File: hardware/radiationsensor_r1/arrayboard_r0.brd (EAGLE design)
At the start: 131.7 x 72.1 mm, 25 parts, among them CN0 RADIATION-SENSOR-REV1, CN1 RADIATION-SENSOR-REV1, CN10 RADIATION-SENSOR-REV1, CN11 RADIATION-SENSOR-REV1, CN12 RADIATION-SENSOR-REV1, CN13 RADIATION-SENSOR-REV1, CN14 RADIATION-SENSOR-REV1, CN15 RADIATION-SENSOR-REV1, CN16 2524-, CN17 22-23-2041, CN2 RADIATION-SENSOR-REV1, CN3 RADIATION-SENSOR-REV1, CN4 RADIATION-SENSOR-REV1, CN5 RADIATION-SENSOR-REV1, CN6 RADIATION-SENSOR-REV1, CN7 RADIATION-SENSOR-REV1, CN8 RADIATION-SENSOR-REV1, CN9 RADIATION-SENSOR-REV1, U1 MCP23017SS

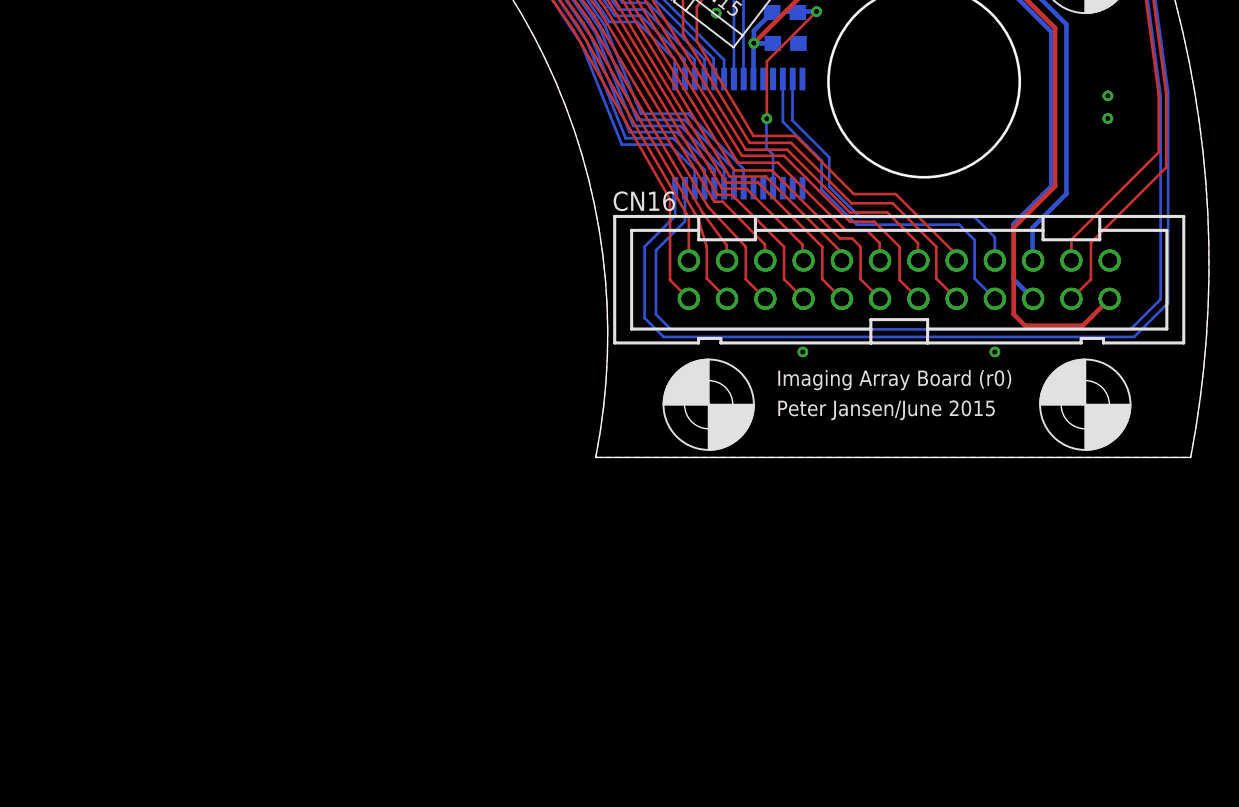
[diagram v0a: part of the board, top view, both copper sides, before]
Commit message: Added MCU to Array board
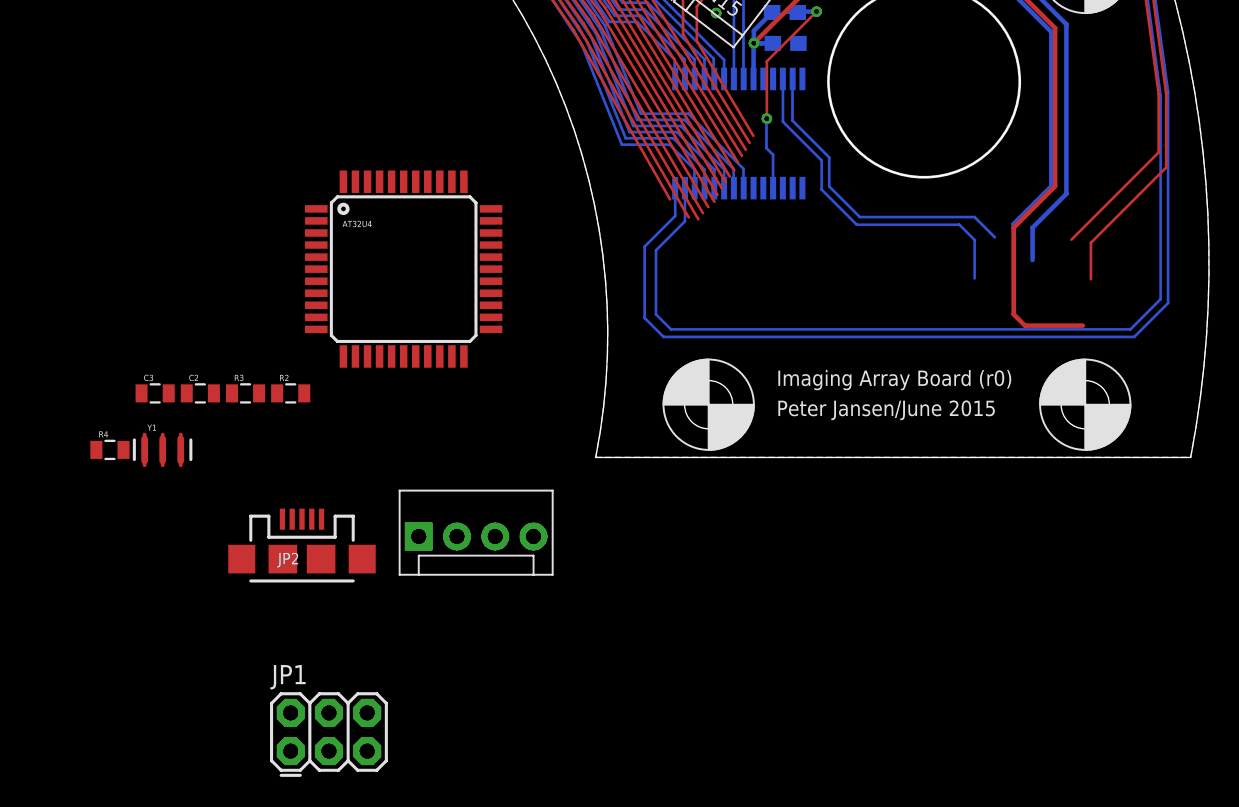
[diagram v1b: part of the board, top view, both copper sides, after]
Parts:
- removed CN16: 2524-, con-3m:PAK100/2500-24
- added AT32U4: ATMEGA32U4TQFP-44, SparkFun-DigitalIC:TQFP44
- added C2: 100nF, SparkFun-Passives:0805
- added C3: 1uF, SparkFun-Passives:0805
- added JP1: AVR_SPI_PRG_6PTH, SparkFun-Connectors:2X3
- added JP2: USB-MICROB, SparkFun-Connectors:USB-MICROB
- added JP3: (no value), SparkFun-Connectors:MOLEX-1X4
- added R2, R3: 22, SparkFun-Passives:0805
- added R4: 10K, SparkFun-Passives:0805
- added Y1: 16MHZ, SparkFun-FreqCtrl:RESONATOR-SMD
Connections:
- removed net COMP1: CN1.6, CN16.2
- new net MISO/COMP1: AT32U4.11, CN1.6, JP1.1
- new net N$1: JP2.D-, R3.1
- new net N$3: JP2.D+, R2.1
- new net N$4: AT32U4.6, C3.2
- new net N$5: AT32U4.17, Y1.1
- new net N$6: AT32U4.2
- new net N$7: AT32U4.16, Y1.3
- new net N$9: AT32U4.42, C2.2
- new net RST: AT32U4.13, JP1.5, R4.1
- new net RX: AT32U4.20, JP3.2
- new net TX: AT32U4.21, JP3.3
- new net USB+: AT32U4.4, R3.2
- new net USB-: AT32U4.3, R2.2
- net COMP0: now also AT32U4.1; no longer CN16.1
- net COMP10: now also AT32U4.31; no longer CN16.11
- net COMP11: now also AT32U4.32; no longer CN16.12
- net COMP12: now also AT32U4.36; no longer CN16.13
- net COMP13: now also AT32U4.37; no longer CN16.14
- net COMP14: now also AT32U4.38; no longer CN16.15
- net COMP15: now also AT32U4.39; no longer CN16.16
- net COMP2: now also AT32U4.12; no longer CN16.3
- net COMP3: now also AT32U4.22; no longer CN16.4
- net COMP4: now also AT32U4.25; no longer CN16.5
- net COMP5: now also AT32U4.26; no longer CN16.6
- net COMP6: now also AT32U4.27; no longer CN16.7
- net COMP7: now also AT32U4.28; no longer CN16.8
- net COMP8: now also AT32U4.29; no longer CN16.9
- net COMP9: now also AT32U4.30; no longer CN16.10
- net GND: now also AT32U4.15, AT32U4.23, AT32U4.35, AT32U4.43, AT32U4.5, C2.1, C3.1, JP1.6, JP2.GND, JP2.MT1, JP2.MT2, JP3.4, Y1.2; no longer CN16.24
- net MOSI: now also AT32U4.10, JP1.4; no longer CN16.20
- net SCL: now also AT32U4.18; no longer CN16.17
- net SCLK: now also AT32U4.9, JP1.3; no longer CN16.19
- net SDA: now also AT32U4.19; no longer CN16.18
- net VLOGIC: now also AT32U4.14, AT32U4.24, AT32U4.34, AT32U4.44, AT32U4.7, JP1.2, JP2.VBUS, JP3.1, R4.2; no longer CN16.23
- net VTEMP11: now also AT32U4.41; no longer CN16.22
- net VTEMP4: now also AT32U4.40; no longer CN16.21
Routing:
- net COMP1: track 99.4 -> 0.00 mm
- net MISO/COMP1: track 0.00 -> 96.5 mm
- net COMP14: track 49.7 -> 30.5 mm
- net COMP15: track 45.6 -> 28.5 mm
- net COMP12: track 55.5 -> 38.6 mm
- net COMP13: track 49.8 -> 34.7 mm
- net COMP10: track 61.8 -> 47.4 mm
- net COMP11: track 55.7 -> 42.9 mm
- net COMP8: track 71.3 -> 59.1 mm
- net COMP9: track 63.3 -> 53.2 mm
- net COMP6: track 79.7 -> 69.9 mm
- net COMP7: track 72.3 -> 64.4 mm
- net COMP4: track 88.4 -> 80.8 mm
- net COMP0: track 106.6 -> 99.4 mm
- net COMP2: track 97.4 -> 91.5 mm
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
